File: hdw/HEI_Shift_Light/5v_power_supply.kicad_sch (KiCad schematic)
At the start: 18 parts

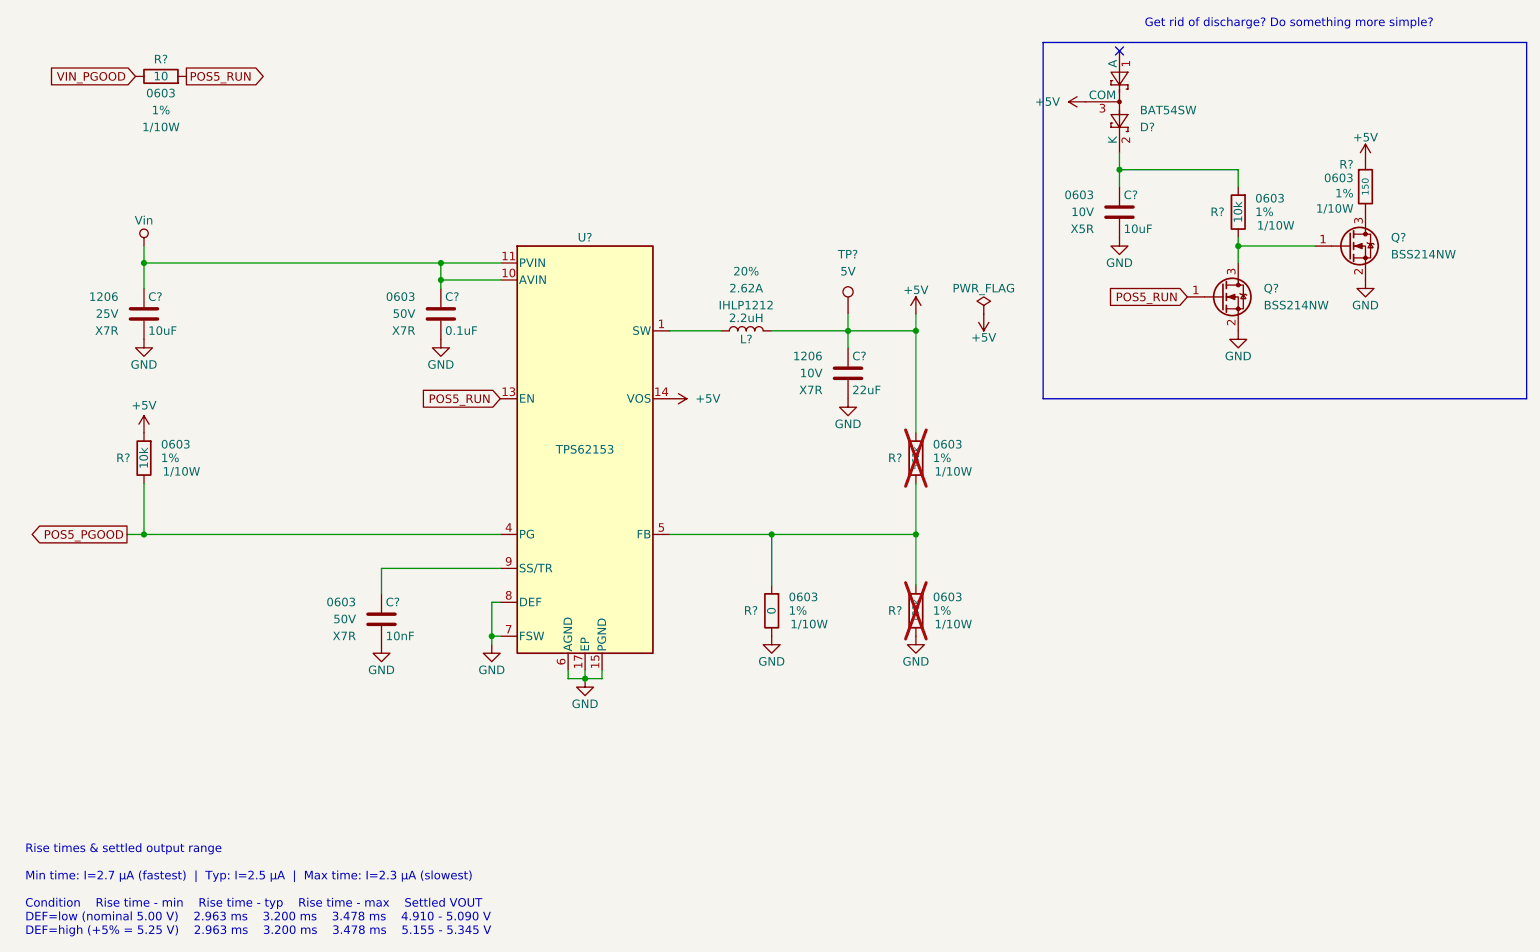
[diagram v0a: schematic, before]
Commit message: filled in digikey part numbers
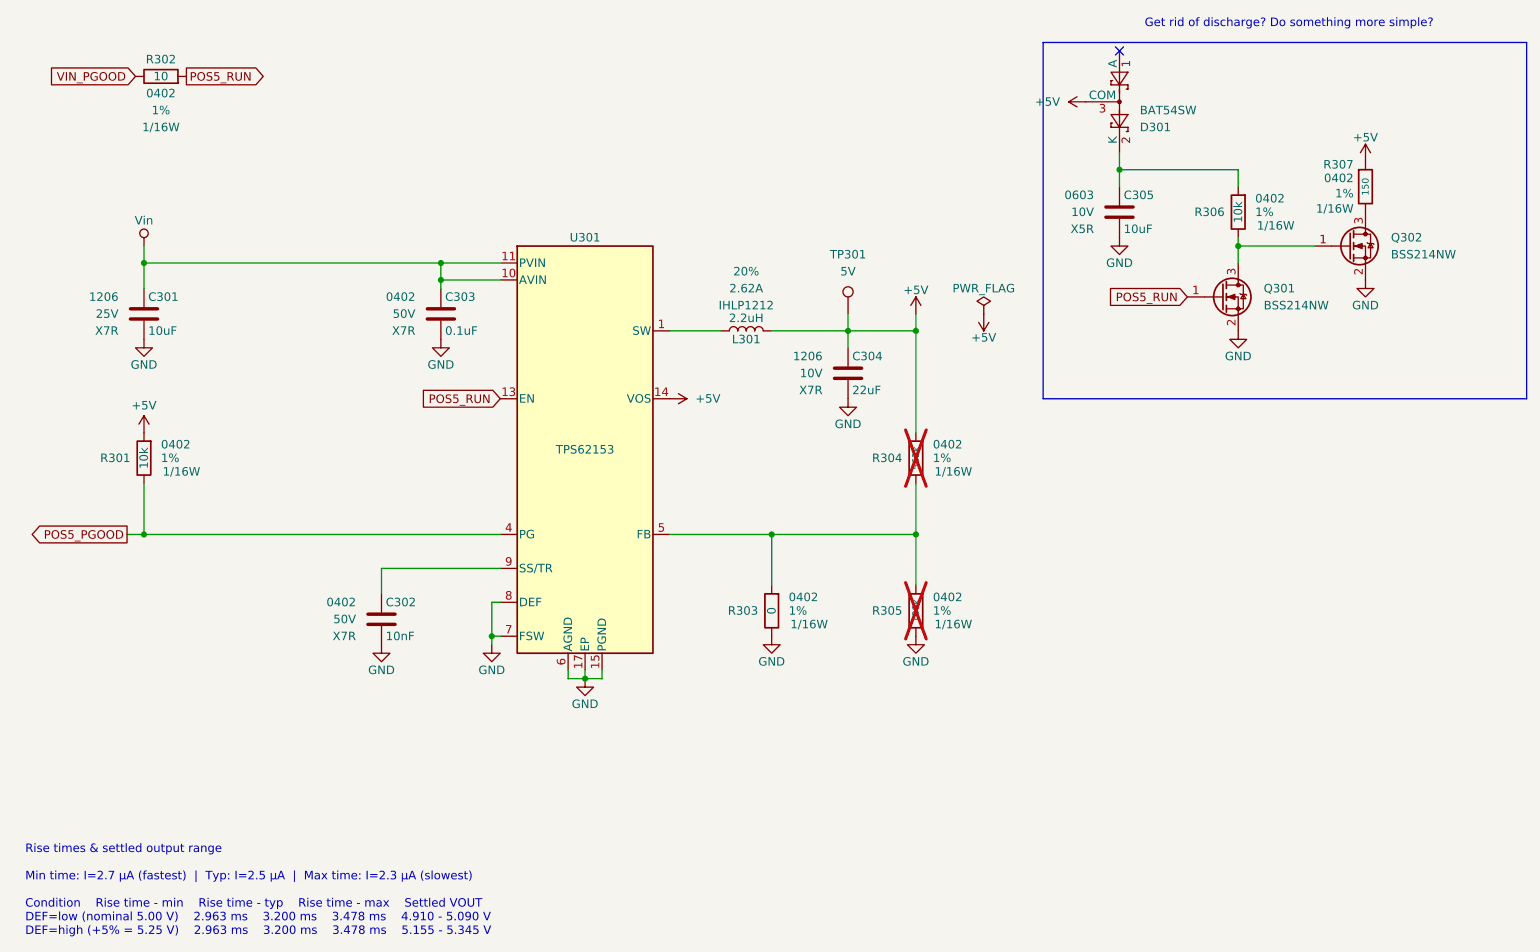
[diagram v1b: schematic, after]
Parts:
- C302, C303: renamed from C?; footprint Capacitors_SMD:C_0603 -> Capacitors_SMD:C_0402; display_footprint 0603 -> 0402
- C304: renamed from C?; footprint (none) -> Capacitors_SMD:C_1206
- D301: renamed from D?; Digi-Key PN (none) -> 568-1615-1-ND
- Q301, Q302: renamed from Q?; Digi-Key PN (none) -> BSS214NWH6327XTSA1CT-ND
- R301, R306: renamed from R?; footprint Resistors_SMD:R_0603 -> Resistors_SMD:R_0402; Digi-Key PN YAG2321CT-ND -> 541-10.0KLCT-ND; Wattage 1/10W -> 1/16W; display_footprint 0603 -> 0402
- R302: renamed from R?; footprint Resistors_SMD:R_0603 -> Resistors_SMD:R_0402; Digi-Key PN YAG2321CT-ND -> 541-10.0LCT-ND; Wattage 1/10W -> 1/16W; display_footprint 0603 -> 0402
- R303: renamed from R?; footprint Resistors_SMD:R_0603 -> Resistors_SMD:R_0402; Digi-Key PN (none) -> 541-0.0JCT-ND; Wattage 1/10W -> 1/16W; display_footprint 0603 -> 0402
- R304: renamed from R?; footprint Resistors_SMD:R_0603 -> Resistors_SMD:R_0402; Digi-Key PN 311-562KHRCT-ND -> 541-562KLCT-ND; Wattage 1/10W -> 1/16W; display_footprint 0603 -> 0402
- R305: renamed from R?; footprint Resistors_SMD:R_0603 -> Resistors_SMD:R_0402; Digi-Key PN 311-180KHRCT-ND -> 541-4071-1-ND; Wattage 1/10W -> 1/16W; display_footprint 0603 -> 0402
- R307: renamed from R?; footprint (none) -> Resistors_SMD:R_0402; Digi-Key PN (none) -> 541-4004-1-ND; Wattage 1/10W -> 1/16W; display_footprint 0603 -> 0402
- U301: renamed from U?; Digi-Key PN (none) -> 296-30010-1-ND
- gave numbers to parts that had none: 4

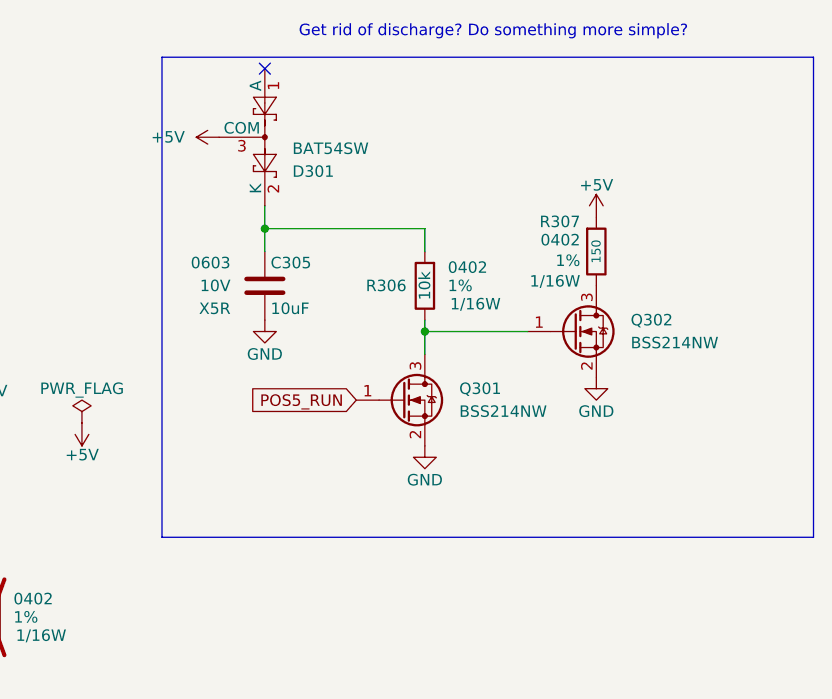
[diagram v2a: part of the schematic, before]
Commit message: fixed some digikey pns
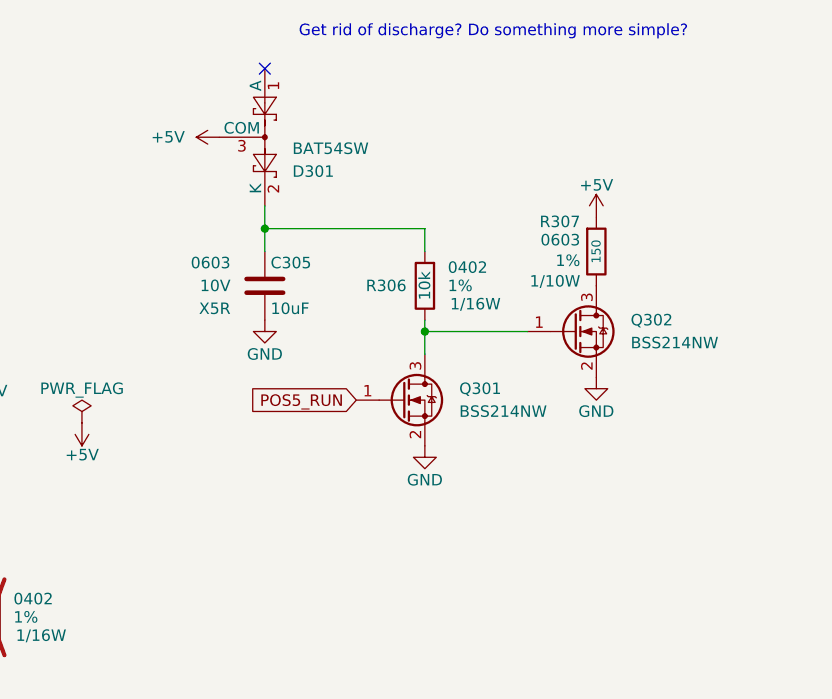
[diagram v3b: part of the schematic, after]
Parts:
- C302: Digi-Key PN 399-7842-1-ND -> 1276-1028-1-ND
- C303: Digi-Key PN 399-7845-1-ND -> 1276-7069-1-ND
- C304: Digi-Key PN (none) -> 1276-3148-1-ND
- R307: footprint Resistors_SMD:R_0402 -> Resistors_SMD:R_0603; Digi-Key PN 541-4004-1-ND -> 541-4023-1-ND; Wattage 1/16W -> 1/10W; display_footprint 0402 -> 0603
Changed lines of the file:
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@@
 		(company "Drew Maatman")
-	)
-	(rectangle
-		(start 193.04 24.13)
-		(end 265.43 77.47)
-		(stroke
-			(width 0)
-			(type solid)
-			(color 0 0 72 1)
-		)
-		(fill
-			(type hatch)
-			(color 0 0 255 1)
-		)
 	)
 	(text "Rise times & settled output range\n\nMin time: I=2.7 µA (fastest)  |  Typ: I=2.5 µA  |  Max time: I=2.3 µA (slowest)\n\nCondition	Rise time - min	Rise time - typ	Rise time - max	Settled VOUT\nDEF=low (nominal 5.00 V)	2.963 ms	3.200 ms	3.478 ms	4.910 - 5.090 V\nDEF=high (+5% = 5.25 V)	2.963 ms	3.200 ms	3.478 ms	5.155 - 5.345 V"
@@
 			)
 		)
-		(property "Digi-Key PN" "399-7845-1-ND"
+		(property "Digi-Key PN" "1276-7069-1-ND"
 			(at 113.665 52.07 0)
 			(hide yes)
@@
 			)
 		)
-		(property "Digi-Key PN" ""
+		(property "Digi-Key PN" "1276-3148-1-ND"
 			(at 163.83 73.66 0)
 			(hide yes)
@@
 				(path "/288c8230-69eb-4ad9-929d-f4630114196f/41605f50-4a5f-4515-812e-3b7b65ea4a04"
 					(reference "#PWR0316")
+					(unit 1)
+				)
+			)
+		)
+	)
+	(symbol
+		(lib_id "Custom_Library:R_Custom")
+		(at 241.3 45.72 0)
+		(mirror y)
+		(unit 1)
+		(body_style 1)
+		(exclude_from_sim no)
+		(in_bom yes)
+		(on_board yes)
+		(in_pos_files yes)
+		(dnp no)
+		(property "Reference" "R307"
+			(at 239.522 42.418 0)
+			(show_name no)
+			(do_not_autoplace no)
+			(effects
+				(font
+					(size 1.27 1.27)
+				)
+				(justify left)
+			)
+		)
+		(property "Value" "150"
+			(at 241.3 45.72 90)
+			(show_name no)
+			(do_not_autoplace no)
+			(effects
+				(font
+					(size 1.016 1.016)
+				)
+			)
+		)
+		(property "Footprint" "Resistors_SMD:R_0603"
+			(at 241.3 45.72 0)
+			(hide yes)
+			(show_name no)
+			(do_not_autoplace no)
+			(effects
+				(font
+					(size 1.27 1.27)
+				)
+			)
+		)
+		(property "Datasheet" ""
+			(at 241.3 45.72 0)
+			(hide yes)
+			(show_name no)
+			(do_not_autoplace no)
+			(effects
+				(font
+					(size 1.27 1.27)
+				)
+			)
+		)
+		(property "Description" ""
+			(at 241.3 45.72 0)
+			(show_name no)
+			(do_not_autoplace no)
+			(effects
+				(font
+					(size 1.27 1.27)
+				)
+			)
+		)
+		(property "display_footprint" "0603"
+			(at 239.522 44.45 0)
+			(show_name no)
+			(do_not_autoplace no)
+			(effects
+				(font
+					(size 1.27 1.27)
+				)
+				(justify left)
+			)
+		)
+		(property "Tolerance" "1%"
+			(at 239.522 46.736 0)
+			(show_name no)
+			(do_not_autoplace no)
+			(effects
+				(font
+					(size 1.27 1.27)
+				)
+				(justify left)
+			)
+		)
+		(property "Wattage" "1/10W"
+			(at 239.522 49.022 0)
+			(show_name no)
+			(do_not_autoplace no)
+			(effects
+				(font
+					(size 1.27 1.27)
+				)
+				(justify left)
+			)
+		)
+		(property "Digi-Key PN" "541-4023-1-ND"
+			(at 241.3 45.72 0)
+			(hide yes)
+			(show_name no)
+			(do_not_autoplace no)
+			(effects
+				(font
+					(size 1.27 1.27)
+				)
+			)
+		)
+		(pin "1"
+		)
+		(pin "2"
+		)
+		(instances
+			(project "HEI_Shift_Light"
+				(path "/288c8230-69eb-4ad9-929d-f4630114196f/41605f50-4a5f-4515-812e-3b7b65ea4a04"
+					(reference "R307")
 					(unit 1)
 				)
@@
 	(symbol
 		(lib_id "Custom_Library:R_Custom")
-		(at 241.3 45.72 0)
-		(mirror y)
-		(unit 1)
-		(body_style 1)
-		(exclude_from_sim no)
-		(in_bom yes)
-		(on_board yes)
-		(in_pos_files yes)
-		(dnp no)
-		(property "Reference" "R307"
-			(at 239.522 42.418 0)
-			(show_name no)
-			(do_not_autoplace no)
-			(effects
-				(font
-					(size 1.27 1.27)
-				)
-				(justify left)
-			)
-		)
-		(property "Value" "150"
-			(at 241.3 45.72 90)
-			(show_name no)
-			(do_not_autoplace no)
-			(effects
-				(font
-					(size 1.016 1.016)
-				)
-			)
-		)
-		(property "Footprint" "Resistors_SMD:R_0402"
-			(at 241.3 45.72 0)
-			(hide yes)
-			(show_name no)
-			(do_not_autoplace no)
-			(effects
-				(font
-					(size 1.27 1.27)
-				)
-			)
-		)
-		(property "Datasheet" ""
-			(at 241.3 45.72 0)
-			(hide yes)
-			(show_name no)
-			(do_not_autoplace no)
-			(effects
-				(font
-					(size 1.27 1.27)
-				)
-			)
-		)
-		(property "Description" ""
-			(at 241.3 45.72 0)
-			(show_name no)
-			(do_not_autoplace no)
-			(effects
-				(font
-					(size 1.27 1.27)
-				)
-			)
-		)
-		(property "display_footprint" "0402"
-			(at 239.522 44.45 0)
-			(show_name no)
-			(do_not_autoplace no)
-			(effects
-				(font
-					(size 1.27 1.27)
-				)
-				(justify left)
-			)
-		)
-		(property "Tolerance" "1%"
-			(at 239.522 46.736 0)
-			(show_name no)
-			(do_not_autoplace no)
-			(effects
-				(font
-					(size 1.27 1.27)
-				)
-				(justify left)
-			)
-		)
-		(property "Wattage" "1/16W"
-			(at 239.522 49.022 0)
-			(show_name no)
-			(do_not_autoplace no)
-			(effects
-				(font
-					(size 1.27 1.27)
-				)
-				(justify left)
-			)
-		)
-		(property "Digi-Key PN" "541-4004-1-ND"
-			(at 241.3 45.72 0)
-			(hide yes)
-			(show_name no)
-			(do_not_autoplace no)
-			(effects
-				(font
-					(size 1.27 1.27)
-				)
-			)
-		)
-		(pin "1"
-		)
-		(pin "2"
-		)
-		(instances
-			(project "HEI_Shift_Light"
-				(path "/288c8230-69eb-4ad9-929d-f4630114196f/41605f50-4a5f-4515-812e-3b7b65ea4a04"
-					(reference "R307")
-					(unit 1)
-				)
-			)
-		)
-	)
-	(symbol
-		(lib_id "Custom_Library:R_Custom")
 		(at 60.96 29.21 270)
 		(unit 1)
@@
 			)
 		)
-		(property "Digi-Key PN" "399-7842-1-ND"
+		(property "Digi-Key PN" "1276-1028-1-ND"
 			(at -5.588 217.678 0)
 			(hide yes)

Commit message: added component datasheet properties
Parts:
- C303: Digi-Key PN 1276-7069-1-ND -> 445-5932-1-ND
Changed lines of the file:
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@@
 			)
 		)
-		(property "Datasheet" ""
+		(property "Datasheet" "https://www.vishay.com/docs/20035/dcrcwe3.pdf"
 			(at 152.4 109.22 0)
 			(hide yes)
@@
 			)
 		)
-		(property "Datasheet" ""
+		(property "Datasheet" "https://product.tdk.com/en/system/files/dam/doc/product/capacitor/ceramic/mlcc/charasheet/c1005x7r1h104k050bb.pdf"
 			(at 103.505 62.23 0)
 			(hide yes)
@@
 			)
 		)
-		(property "Digi-Key PN" "1276-7069-1-ND"
+		(property "Digi-Key PN" "445-5932-1-ND"
 			(at 113.665 52.07 0)
 			(hide yes)
@@
 			)
 		)
-		(property "Datasheet" ""
+		(property "Datasheet" "https://mm.digikey.com/Volume0/opasdata/d220001/medias/docus/41/CL31B226MPHNNNE_Spec.pdf"
 			(at 164.465 71.12 0)
 			(hide yes)
@@
 			)
 		)
-		(property "Datasheet" ""
+		(property "Datasheet" "https://www.vishay.com/docs/20035/dcrcwe3.pdf"
 			(at 241.3 45.72 0)
 			(hide yes)
@@
 			)
 		)
-		(property "Datasheet" ""
+		(property "Datasheet" "https://www.vishay.com/docs/20035/dcrcwe3.pdf"
 			(at 60.96 29.21 0)
 			(hide yes)
@@
 			)
 		)
-		(property "Datasheet" ""
+		(property "Datasheet" "https://www.vishay.com/docs/20035/dcrcwe3.pdf"
 			(at 173.99 86.36 0)
 			(hide yes)
@@
 			)
 		)
-		(property "Datasheet" ""
+		(property "Datasheet" "https://mm.digikey.com/Volume0/opasdata/d220001/medias/docus/609/CL05B103KB5NNN_Spec.pdf"
 			(at 94.615 107.95 0)
 			(hide yes)
@@
 			)
 		)
-		(property "Datasheet" ""
+		(property "Datasheet" "https://www.vishay.com/docs/20035/dcrcwe3.pdf"
 			(at 222.25 49.53 0)
 			(hide yes)
@@
 			)
 		)
-		(property "Datasheet" ""
+		(property "Datasheet" "https://www.vishay.com/docs/34535/ihlp-1212bz-5a.pdf"
 			(at 148.59 67.31 0)
 			(hide yes)
@@
 			)
 		)
-		(property "Datasheet" ""
+		(property "Datasheet" "https://www.vishay.com/docs/20035/dcrcwe3.pdf"
 			(at 58.42 86.36 0)
 			(hide yes)
@@
 			)
 		)
-		(property "Datasheet" ""
+		(property "Datasheet" "https://mm.digikey.com/Volume0/opasdata/d220001/medias/docus/2322/CL31B106KAHZW6E_Spec.pdf"
 			(at 59.055 62.23 0)
 			(hide yes)
@@
 			)
 		)
-		(property "Datasheet" ""
+		(property "Datasheet" "https://search.murata.co.jp/Ceramy/image/img/A01X/G101/ENG/GRM188R61A106KE69-01.pdf"
 			(at 205.105 46.99 0)
 			(hide yes)
@@
 			)
 		)
-		(property "Datasheet" ""
+		(property "Datasheet" "https://www.vishay.com/docs/20035/dcrcwe3.pdf"
 			(at 173.99 109.22 0)
 			(hide yes)

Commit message: updated a lot of font, table of contents
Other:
- note removed: "Get rid of discharge? Do something more simple?"
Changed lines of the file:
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@@
 	(title_block
 		(title "HEI Shift Light")
-		(date "2026-05-29")
+		(date "2026-06-02")
 		(rev "A")
 		(company "Drew Maatman")
@@
 		(effects
 			(font
+				(face "Arial")
 				(size 1.27 1.27)
 			)
@@
 		)
 	)
-	(text "Get rid of discharge? Do something more simple?"
-		(exclude_from_sim no)
-		(at 229.87 21.336 0)
-		(effects
-			(font
-				(size 1.27 1.27)
-			)
-		)
-	)

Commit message: cleaned up digikey pns
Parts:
- C305: Digi-Key PN 490-10474-1-ND -> 445-C1608X5R1A106K080ACCT-ND
- D301: Digi-Key PN 568-1615-1-ND -> BAT54SWT1GOSCT-ND
- Q301, Q302: value BSS214NW -> DMN3150LW-7; Digi-Key PN BSS214NWH6327XTSA1CT-ND -> DMN3150LWDICT-ND
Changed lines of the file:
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@@
 		(shape input)
 		(at 214.63 62.23 180)
+		(fields_autoplaced yes)
 		(effects
 			(font
@@
 		)
 		(property "Intersheetrefs" "${INTERSHEET_REFS}"
-			(at 214.63 62.23 0)
-			(hide yes)
-			(show_name no)
-			(do_not_autoplace no)
-			(effects
-				(font
-					(size 1.27 1.27)
-				)
+			(at 201.7267 62.23 0)
+			(show_name no)
+			(do_not_autoplace no)
+			(effects
+				(font
+					(size 1.27 1.27)
+				)
+				(justify right)
 			)
 		)
@@
 		(shape input)
 		(at 57.15 29.21 180)
+		(fields_autoplaced yes)
 		(effects
 			(font
@@
 		)
 		(property "Intersheetrefs" "${INTERSHEET_REFS}"
-			(at 57.15 29.21 0)
-			(hide yes)
-			(show_name no)
-			(do_not_autoplace no)
-			(effects
-				(font
-					(size 1.27 1.27)
-				)
+			(at 43.7023 29.21 0)
+			(show_name no)
+			(do_not_autoplace no)
+			(effects
+				(font
+					(size 1.27 1.27)
+				)
+				(justify right)
 			)
 		)
@@
 		(shape output)
 		(at 55.88 97.79 180)
+		(fields_autoplaced yes)
 		(effects
 			(font
@@
 		)
 		(property "Intersheetrefs" "${INTERSHEET_REFS}"
-			(at 55.88 97.79 0)
-			(hide yes)
-			(show_name no)
-			(do_not_autoplace no)
-			(effects
-				(font
-					(size 1.27 1.27)
-				)
+			(at 40.4367 97.79 0)
+			(show_name no)
+			(do_not_autoplace no)
+			(effects
+				(font
+					(size 1.27 1.27)
+				)
+				(justify right)
 			)
 		)
@@
 		(shape output)
 		(at 64.77 29.21 0)
+		(fields_autoplaced yes)
 		(effects
 			(font
@@
 		)
 		(property "Intersheetrefs" "${INTERSHEET_REFS}"
-			(at 64.77 29.21 0)
-			(hide yes)
-			(show_name no)
-			(do_not_autoplace no)
-			(effects
-				(font
-					(size 1.27 1.27)
-				)
+			(at 77.6733 29.21 0)
+			(show_name no)
+			(do_not_autoplace no)
+			(effects
+				(font
+					(size 1.27 1.27)
+				)
+				(justify left)
 			)
 		)
@@
 		(shape input)
 		(at 111.76 77.47 180)
+		(fields_autoplaced yes)
 		(effects
 			(font
@@
 		)
 		(property "Intersheetrefs" "${INTERSHEET_REFS}"
-			(at 111.76 77.47 0)
-			(hide yes)
-			(show_name no)
-			(do_not_autoplace no)
-			(effects
-				(font
-					(size 1.27 1.27)
-				)
+			(at 98.8567 77.47 0)
+			(show_name no)
+			(do_not_autoplace no)
+			(effects
+				(font
+					(size 1.27 1.27)
+				)
+				(justify right)
 			)
 		)
@@
 			)
 		)
-		(property "Value" "BSS214NW"
+		(property "Value" "DMN3150LW-7"
 			(at 226.06 63.4999 0)
 			(show_name no)
@@
 			)
 		)
-		(property "Digi-Key PN" "BSS214NWH6327XTSA1CT-ND"
+		(property "Digi-Key PN" "DMN3150LWDICT-ND"
 			(at 219.71 62.23 0)
 			(hide yes)
@@
 			)
 		)
-		(property "Digi-Key PN" "568-1615-1-ND"
+		(property "Digi-Key PN" "BAT54SWT1GOSCT-ND"
 			(at 204.47 33.02 0)
 			(hide yes)
@@
 			)
 		)
-		(property "Digi-Key PN" "490-10474-1-ND"
+		(property "Digi-Key PN" "445-C1608X5R1A106K080ACCT-ND"
 			(at 204.47 49.53 0)
 			(hide yes)
@@
 			)
 		)
-		(property "Value" "BSS214NW"
+		(property "Value" "DMN3150LW-7"
 			(at 245.11 55.8799 0)
 			(show_name no)
@@
 			)
 		)
-		(property "Digi-Key PN" "BSS214NWH6327XTSA1CT-ND"
+		(property "Digi-Key PN" "DMN3150LWDICT-ND"
 			(at 238.76 54.61 0)
 			(hide yes)

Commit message: fixed some footprints, pulled into PCB
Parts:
- U301: footprint Package_DFN_QFN:QFN-16-1EP_3x3mm_P0.5mm_EP1.8x1.8mm -> Package_DFN_QFN:QFN-16-1EP_3x3mm_P0.5mm_EP1.675x1.675mm
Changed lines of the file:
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@@
 			)
 		)
-		(property "Footprint" "Package_DFN_QFN:QFN-16-1EP_3x3mm_P0.5mm_EP1.8x1.8mm"
+		(property "Footprint" "Package_DFN_QFN:QFN-16-1EP_3x3mm_P0.5mm_EP1.675x1.675mm"
 			(at 124.46 85.09 0)
 			(hide yes)
